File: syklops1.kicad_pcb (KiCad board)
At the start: 2 copper layers, 40 x 48 mm, 38 parts, among them J1 MCU_I2C, J2 USB_C_Receptacle_PowerOnly_6P, J3 Conn_01x06, J4 Conn_01x08, J6 Conn_01x04

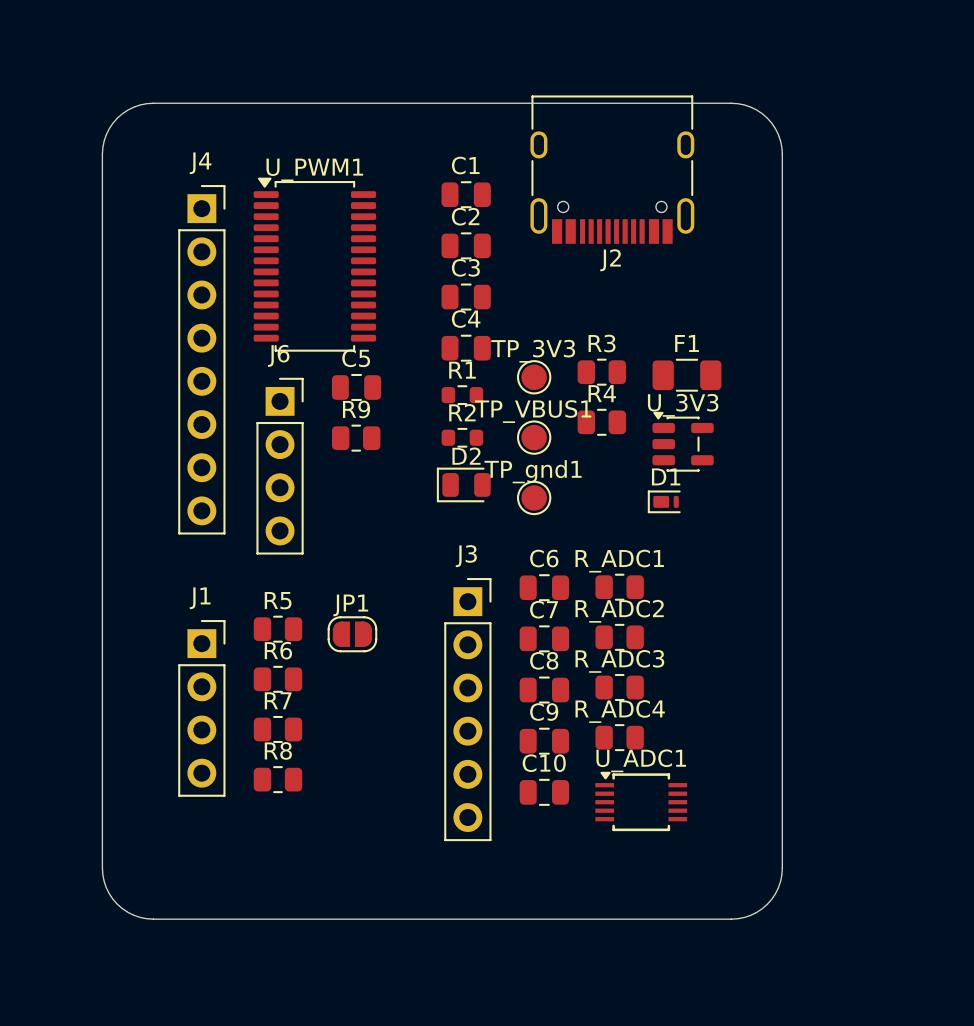
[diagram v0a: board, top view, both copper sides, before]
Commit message: Add files via upload
v3 : almost complete PCB layout, one common GND instance missing, USB-C footprint without BOM
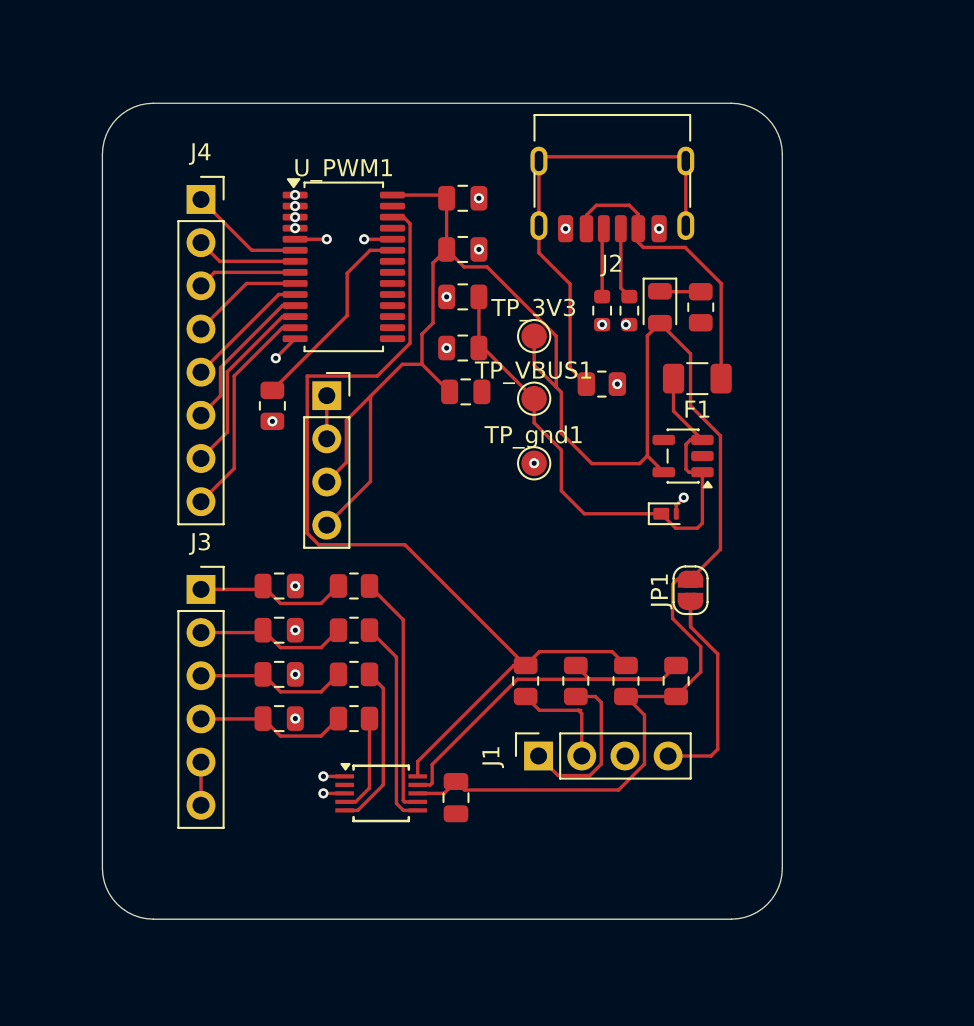
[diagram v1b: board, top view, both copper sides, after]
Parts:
- J2: footprint Connector_USB:USB_C_Receptacle_HRO_TYPE-C-31-M-12 -> Connector_USB:USB_C_Receptacle_HRO_TYPE-C-31-M-17
- moved R8 24.1 mm to (66.8, 65.0), turned to 90 degrees
- moved J1 20.9 mm to (58.7, 69.4), turned to 90 degrees
- moved R7 20.7 mm to (63.8, 65.0), turned to 90 degrees
- moved JP1 20.1 mm to (67.6, 59.6), turned to 90 degrees
- moved R6 17.5 mm to (60.9, 65.0), turned to -90 degrees
- moved C10 17.1 mm to (43.4, 64.6)
- moved C9 16.9 mm to (43.4, 62.0), turned to 180 degrees
- moved C8 16.8 mm to (43.4, 59.4)
- moved C7 16.3 mm to (43.4, 67.2), turned to 180 degrees
- moved J3 15.7 mm to (38.8, 59.6)
- moved R_ADC4 15.7 mm to (47.8, 67.2)
- moved R_ADC3 15.6 mm to (47.8, 64.6), turned to 180 degrees
- moved R_ADC2 15.6 mm to (47.8, 62.0), turned to 180 degrees
- moved R_ADC1 15.6 mm to (47.8, 59.4), turned to 180 degrees
- moved D2 15.5 mm to (65.8, 43.0), turned to -90 degrees
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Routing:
- net Vlogic_3V3: track 0.00 -> 116.5 mm
- net SCL_BUS: track 0.00 -> 56.5 mm
- net VBUS_5V: track 0.00 -> 33.8 mm
- net Net-(J2-SHIELD): track 0.00 -> 27.3 mm
- net SDA_BUS: track 0.00 -> 24.2 mm
- net Net-(F1-Pad1): track 0.00 -> 17.4 mm
- net /MCU_interface/MCU_3V3: track 0.00 -> 14.5 mm
- net Net-(U_ADC1-AIN3): track 0.00 -> 14.3 mm
- net GND: track 0.00 -> 13.9 mm, vias 0 -> 29
- net /PWM/PWM7: track 0.00 -> 13.0 mm
- net Net-(U_ADC1-AIN2): track 0.00 -> 12.3 mm
- net Net-(U_PWM1-~{OE}): track 0.00 -> 11.9 mm
- net /PWM/PWM6: track 0.00 -> 11.1 mm
- net Net-(U_ADC1-AIN1): track 0.00 -> 9.73 mm
- net /MCU_interface/SDA_MCU: track 0.00 -> 9.72 mm
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
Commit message: Add files via upload
V4 : completed and working PCB. now zero DRC errors yet. room for refinement but working.
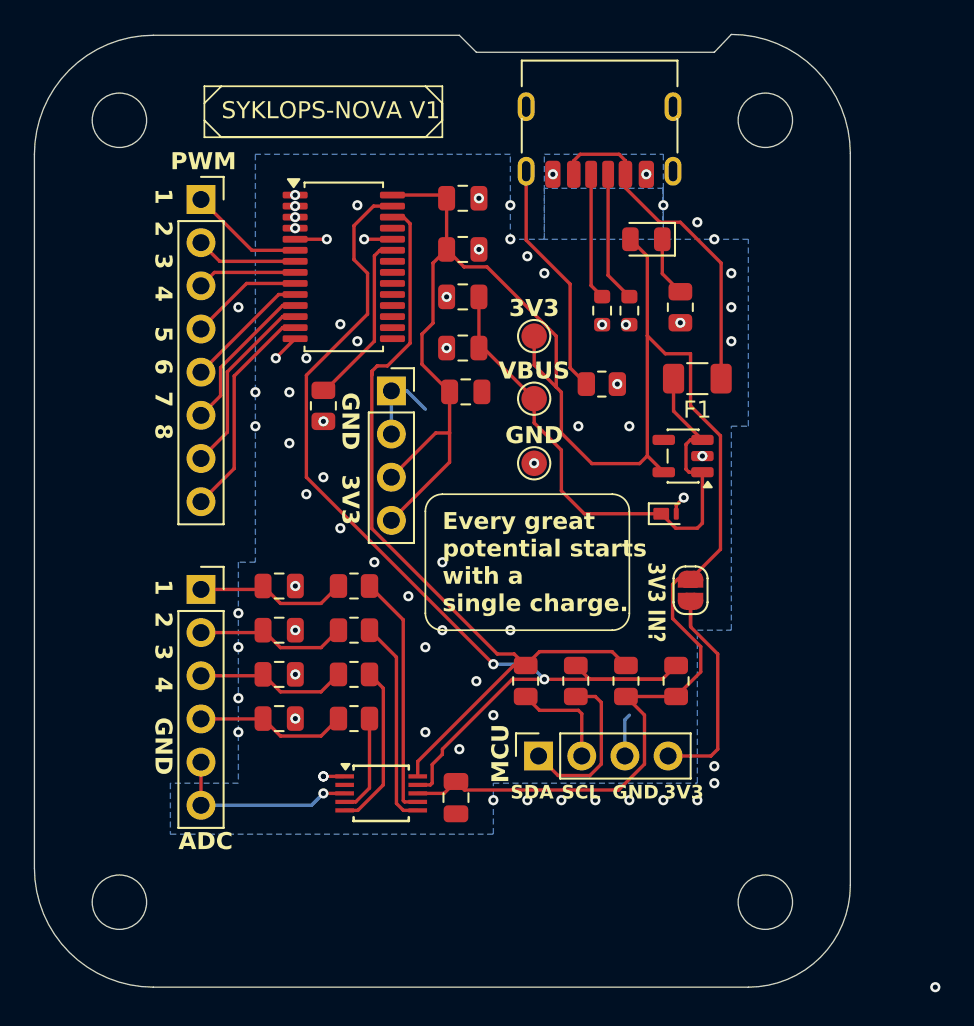
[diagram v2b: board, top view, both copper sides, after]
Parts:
- added REF**: MountingHole_3.2mm_M3, MountingHole:MountingHole_3.2mm_M3, F.Cu at (34.0, 78.0)
- added REF**: MountingHole_3.2mm_M3, MountingHole:MountingHole_3.2mm_M3, F.Cu at (72.0, 78.0)
- added REF**: MountingHole_3.2mm_M3, MountingHole:MountingHole_3.2mm_M3, F.Cu at (72.0, 32.0)
- added REF**: MountingHole_3.2mm_M3, MountingHole:MountingHole_3.2mm_M3, F.Cu at (34.0, 32.0)
- moved D2 4.08 mm to (65.0, 39.0), turned to 180 degrees
- moved J6 3.81 mm to (50.0, 47.9)
- moved J2 3.29 mm to (62.2, 32.0)
- moved R9 3.00 mm to (46.0, 48.8)
- moved R4 1.20 mm to (67.0, 43.0)
- renumbered TP_3V3 to 3V3, TP_gnd1 to GND, J4 to J_PWM, TP_VBUS1 to VBUS
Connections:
- R4 pad 1: Net-(U_3V3-GND) -> GND
- U_3V3 pad 2: Net-(U_3V3-GND) -> GND
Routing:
- net SDA_BUS: track 24.2 -> 62.6 mm, vias 0 -> 2
- net Net-(J2-SHIELD): track 27.3 -> 14.0 mm
- net GND: track 13.9 -> 26.3 mm, vias 29 -> 33
- net SCL_BUS: track 56.5 -> 49.2 mm
- net Net-(J2-CC1): track 4.56 -> 8.07 mm
- net Net-(J2-CC2): track 4.04 -> 7.46 mm
- net Net-(F1-Pad1): track 17.4 -> 20.0 mm
- net Net-(U_PWM1-~{OE}): track 11.9 -> 10.4 mm
- net Net-(D2-K): track 2.41 -> 3.53 mm
- net (no net): vias 0 -> 48
- added copper zone on B.Cu, net GND
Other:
- board size 40 x 48 mm -> 48 x 56.1 mm
- board text added: "1 2 3 4 5 6 7 8"
- board text added: "1 2 3 4 GND"
- board text added: "3V3"
- board text added: "3V3 IN?"
- board text added: "ADC"
- board text added: "Every great potential starts with a single charge."
- board text added: "GND"
- board text added: "GND 3V3"
- board text added: "MCU"
- board text added: "PWM"
- board text added: "SCL"
- board text added: "SDA"
- board text added: "SYKLOPS-NOVA V1"

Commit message: Add files via upload
V4 : full and final v1.1. Working schematics. Working PCB layout, zero ERC and DRC errors and warnings(except for cosmetic ones).
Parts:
- moved D2 1.00 mm to (65.0, 38.0)
- moved J2 0.32 mm to (62.0, 31.8)
- renumbered J_PWM to J4, 3V3 to TP_3V3, VBUS to TP_VBUS1, GND to TP_gnd1
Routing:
- net GND: track 26.3 -> 54.0 mm, vias 33 -> 30
- net Net-(J2-SHIELD): track 14.0 -> 30.5 mm
- net Vlogic_3V3: track 116.9 -> 117.9 mm
- net Net-(D2-K): track 3.53 -> 4.53 mm
- net Net-(F1-Pad1): track 20.0 -> 20.7 mm
- net (no net): vias 48 -> 46
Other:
- board text added: "5V"
- board text added: "POWER"
